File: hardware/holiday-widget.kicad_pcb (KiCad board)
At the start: 4 copper layers, 108.4 x 65.8 mm, 149 parts, among them J2 UART, J33 Conn_ARM_JTAG_SWD_10, J4 BATTERY POWER, J7 Speaker, Q1 MMBT3906, Q10 MMBT3906, Q11 MMBT3906, Q12 MMBT3906, Q18 MMBT3906, Q19 MMBT3906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

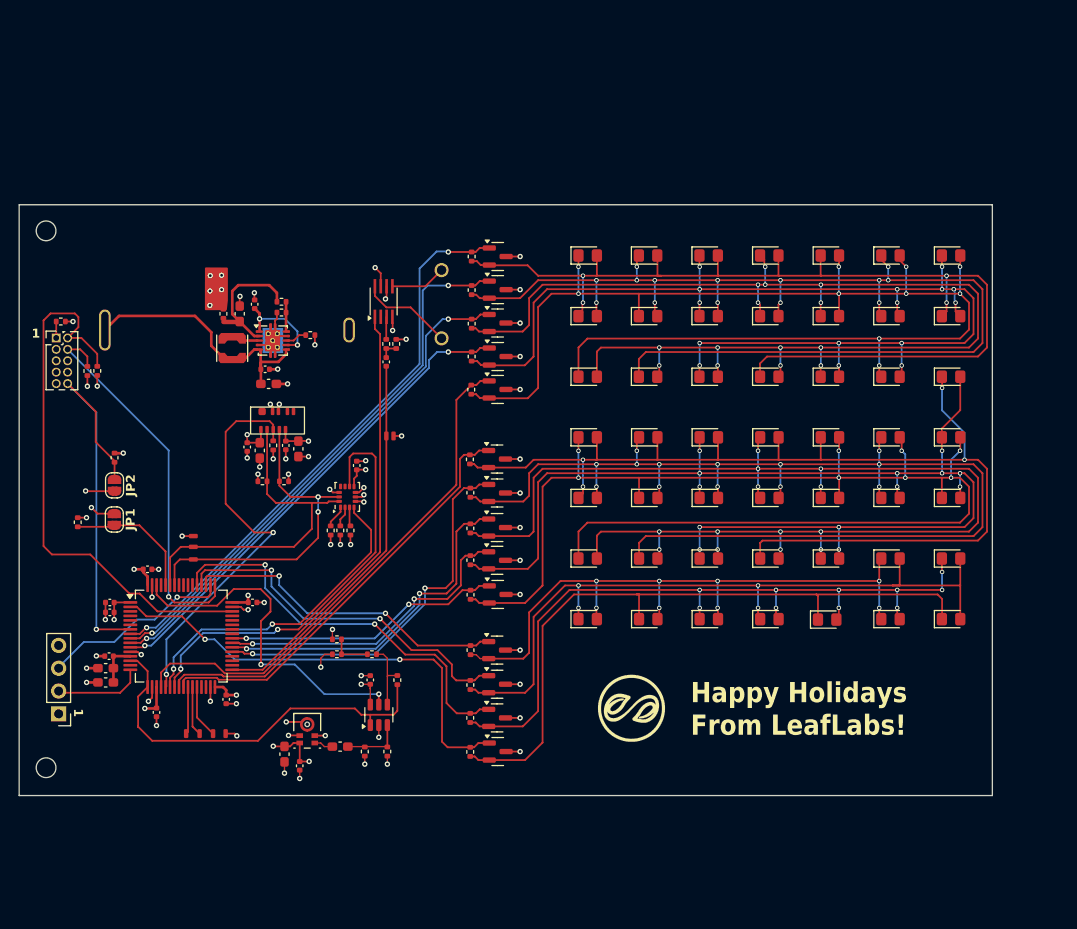
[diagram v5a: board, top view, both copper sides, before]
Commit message: New hexagon routing.
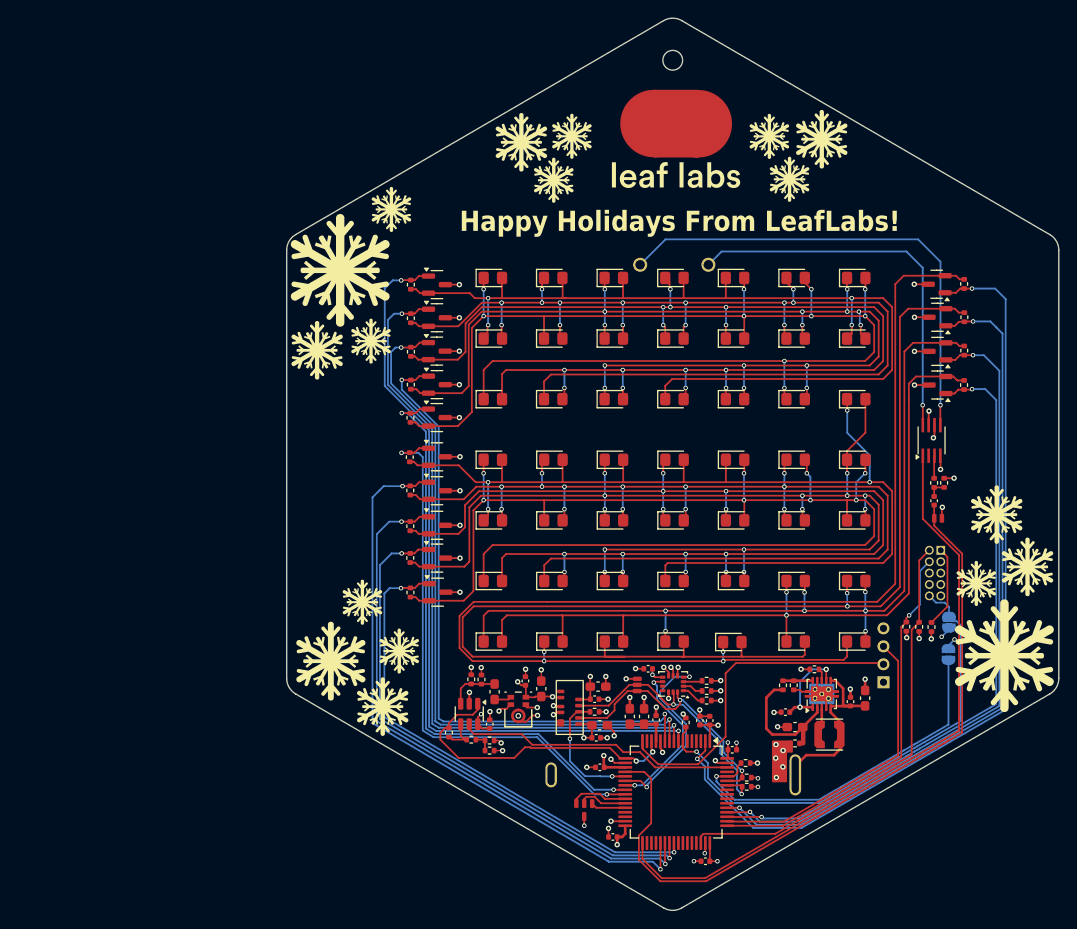
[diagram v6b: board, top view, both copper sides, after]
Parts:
- removed G***: LOGO, Leaf_Mechanical:leaf_logo_small
- removed the REF** at (130.2, 133.8)
- J2: footprint Connector_PinHeader_2.54mm:PinHeader_1x04_P2.54mm_Vertical -> Connector_PinHeader_2.00mm:PinHeader_1x04_P2.00mm_Vertical; moved to B.Cu
- J33, JP1, JP2: moved to B.Cu
- moved R24 102.8 mm to (228.8, 118.1), turned to 90 degrees
- moved J33 101.3 mm to (229.8, 109.6), turned to 180 degrees
- moved R26 95.9 mm to (227.4, 118.1)
- moved R25 95.6 mm to (226.0, 118.1)
- moved JP2 94.2 mm to (230.8, 117.6)
- moved JP1 94.1 mm to (230.7, 121.2)
- moved J2 91.9 mm to (223.5, 124.3), turned to 0 degrees
- moved R14 79.6 mm to (213.6, 131.1), turned to 180 degrees
- moved L1 79.2 mm to (217.5, 130.1), turned to 180 degrees
- moved R3 79.1 mm to (208.1, 133.3), turned to 0 degrees
- moved C11 77.1 mm to (213.6, 129.3), turned to 180 degrees
- moved R36 75.8 mm to (232.5, 79.9), turned to -90 degrees
- moved C23 75.1 mm to (221.4, 126.1), turned to 90 degrees
- moved C9 75.0 mm to (219.8, 126.4), turned to 90 degrees
- moved C10 74.6 mm to (212.6, 127.6), turned to 180 degrees
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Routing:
- net /Input and Output/LED Output2/CTRL3: track 76.3 -> 145.2 mm, vias 0 -> 4
- net /Input and Output/LED Output2/CTRL2: track 80.6 -> 141.3 mm, vias 10 -> 2
- net Net-(J7-Pin_1): track 6.22 -> 53.9 mm, vias 0 -> 1
- net /mcu/LED13: track 51.5 -> 97.4 mm
- net /mcu/LED12: track 45.2 -> 83.7 mm
- net /mcu/LED11: track 40.5 -> 78.5 mm
- net /mcu/LED10: track 36.4 -> 73.7 mm
- net Net-(J7-Pin_2): track 10.5 -> 42.8 mm, vias 0 -> 1
- net /Sensors/VCNL4020_INT: track 44.5 -> 14.1 mm
- net /Sensors/IMU_INT2: track 47.4 -> 17.6 mm
- net /mcu/LED6: track 42.9 -> 71.6 mm
- net /UART.TX: track 9.69 -> 37.3 mm
- net /mcu/LED7: track 38.8 -> 66.3 mm
- net /Input and Output/AUDIO_OUT: track 53.5 -> 80.9 mm
- net /mcu/LED8: track 35.0 -> 61.5 mm
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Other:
- board size 108.4 x 65.8 mm -> 86 x 99.4 mm
- board text added: "Holiday Widget 2024"
- board text removed: "Holiday Widget v2.1"
